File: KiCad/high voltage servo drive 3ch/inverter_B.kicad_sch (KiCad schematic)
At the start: 50 parts, among them U17 IPM

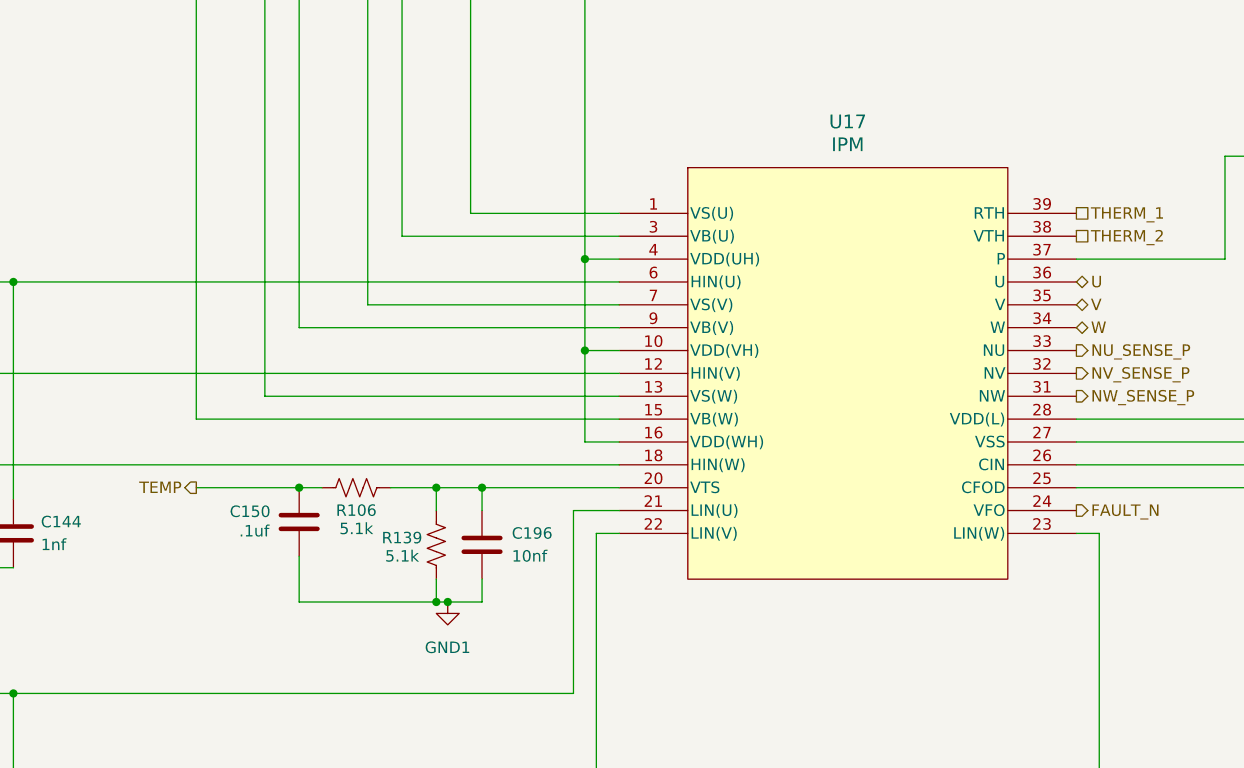
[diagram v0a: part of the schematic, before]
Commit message: add rev 0.2 changes and rev 0.1 mfg files
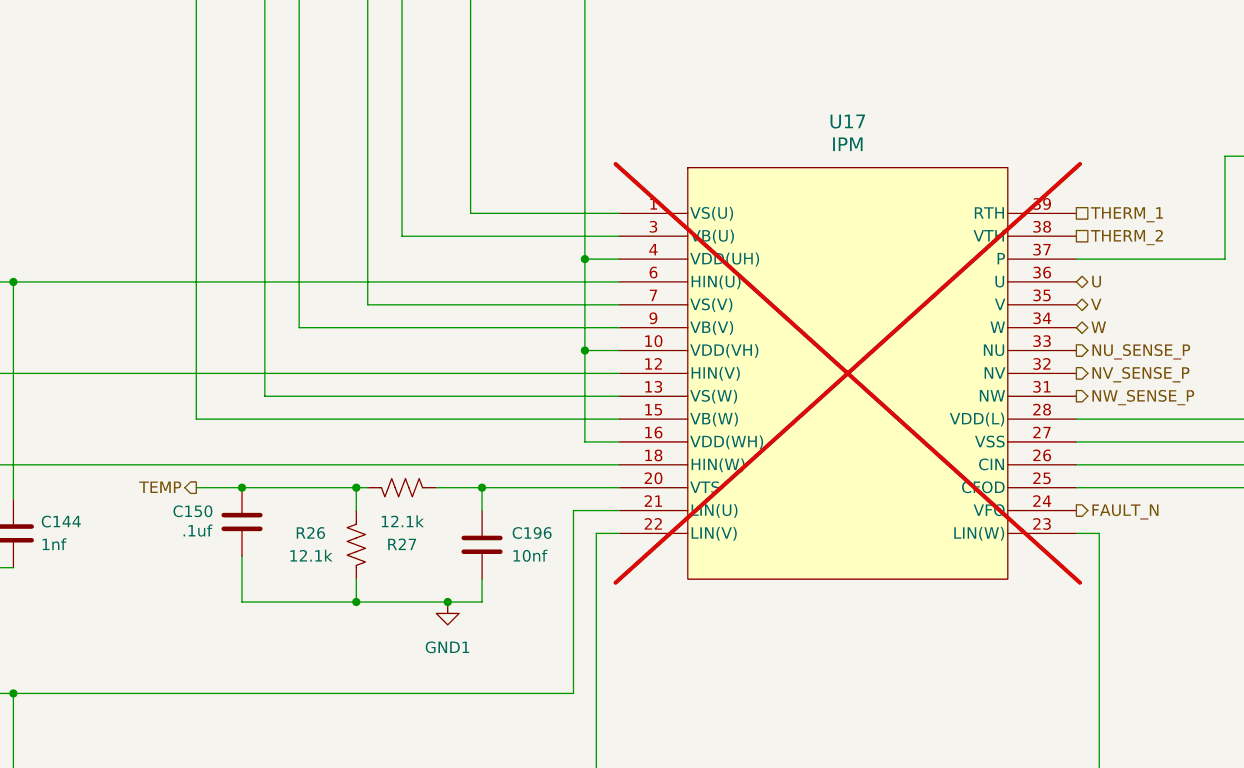
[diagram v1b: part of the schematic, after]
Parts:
- removed R106, R139: 5.1k, Resistor_SMD:R_0402_1005Metric, symbol Device:R_US
- added R26, R27: 12.1k, Resistor_SMD:R_0402_1005Metric, symbol Device:R_US
- U17: footprint DIP39_54.5X31.0_MODGC_OSI -> footprints:DIP39_54.5X31.0_MODGC_OSI; Generic Allowed? (none) -> no; now not fitted
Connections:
- net GND1: now also R26.2
- net TEMP: now also R26.1, R27.1
- net at C196.1, U17.20 (VTS): now also R27.2
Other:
- moved on the sheet: C150
